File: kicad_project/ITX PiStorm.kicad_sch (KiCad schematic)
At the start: 10 parts, among them J2 USB_67298-4090, J3 DB9_Male_MountingHoles, J4 DB9_Male_MountingHoles, J5 HDMI_A_1.4, J6 DB15_Female_HighDensity

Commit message: playground start
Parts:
- added U101: (no value), symbol Memory_Flash:W25Q128JVS
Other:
- sheet Power Supply ports: added +12V, +5V, GND; removed none

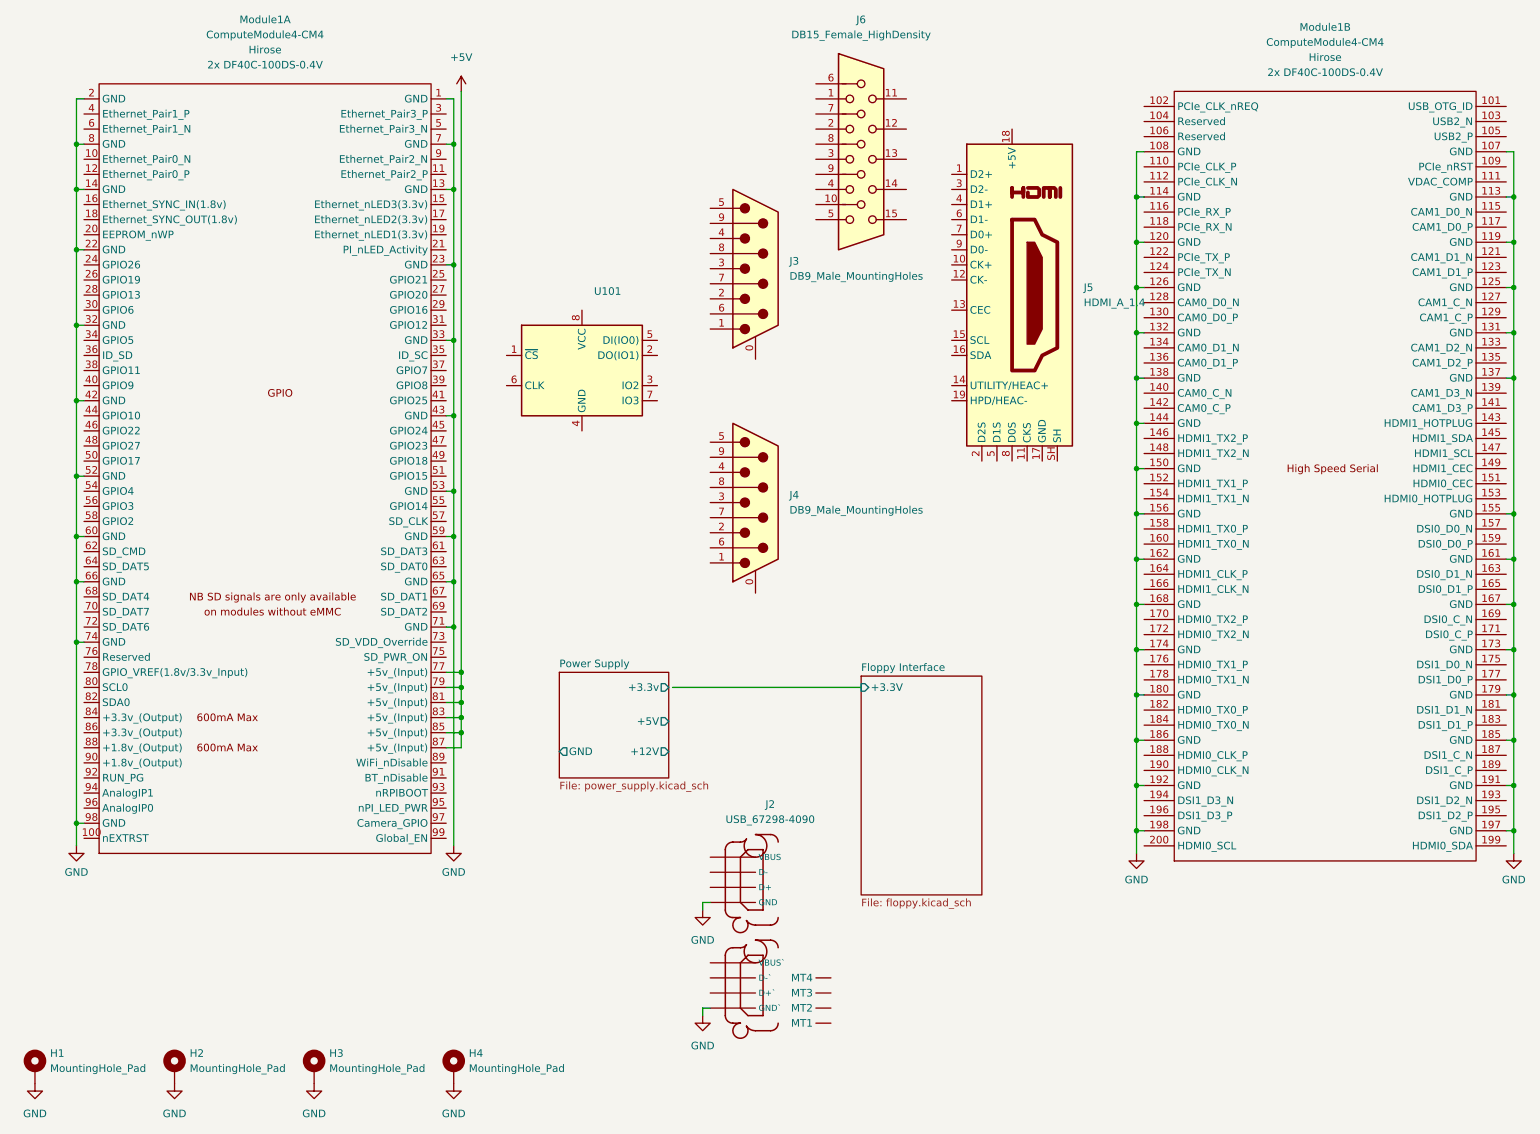
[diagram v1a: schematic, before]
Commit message: added ecp5 fpga without anything connected yet, added power to fpga
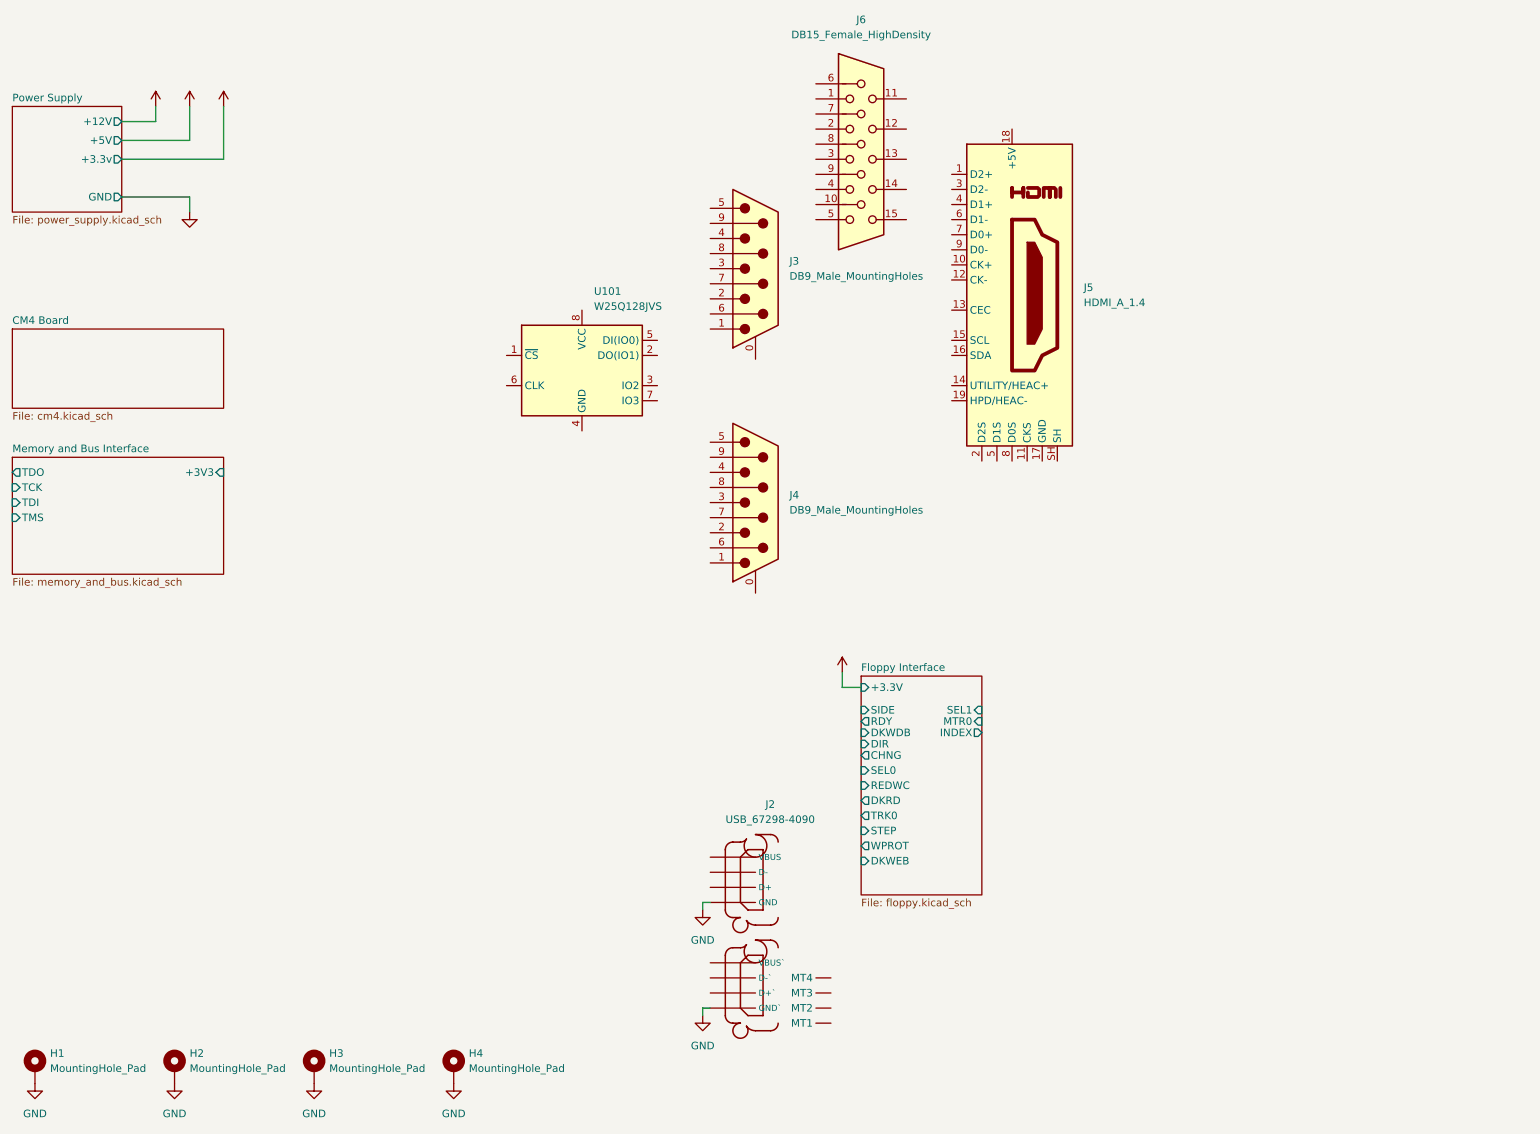
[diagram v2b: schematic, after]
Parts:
- removed Module1: ComputeModule4-CM4, CM4IO:Raspberry-Pi-4-Compute-Module, symbol CM4IO:ComputeModule4-CM4
- U101: value (none) -> W25Q128JVS; footprint (none) -> Package_SO:SOIC-8_5.23x5.23mm_P1.27mm
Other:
- added sheet CM4 Board (cm4.kicad_sch)
- added sheet Memory and Bus Interface (memory_and_bus.kicad_sch)
- sheet Floppy Interface ports: added CHNG, DIR, DKRD, DKWDB, DKWEB, INDEX, MTR0, RDY, REDWC, SEL0, SEL1, SIDE, STEP, TRK0, WPROT; removed none

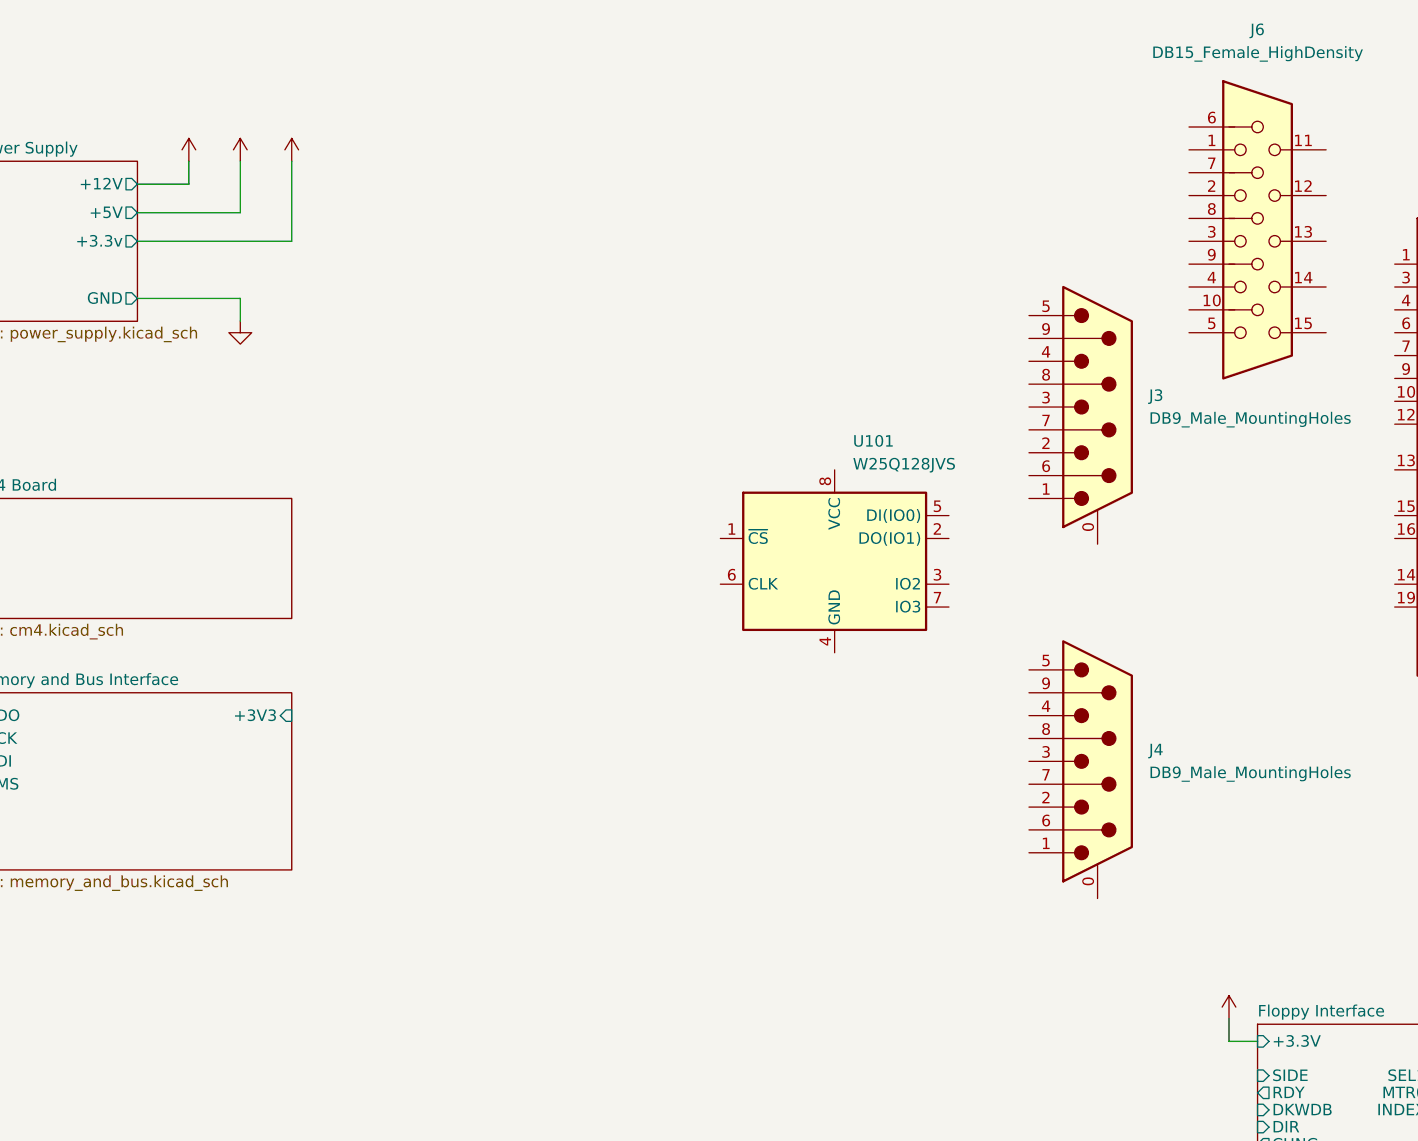
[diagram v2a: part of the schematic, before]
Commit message: added bits and pieces: a bit of memory, a bit of 1.1V power
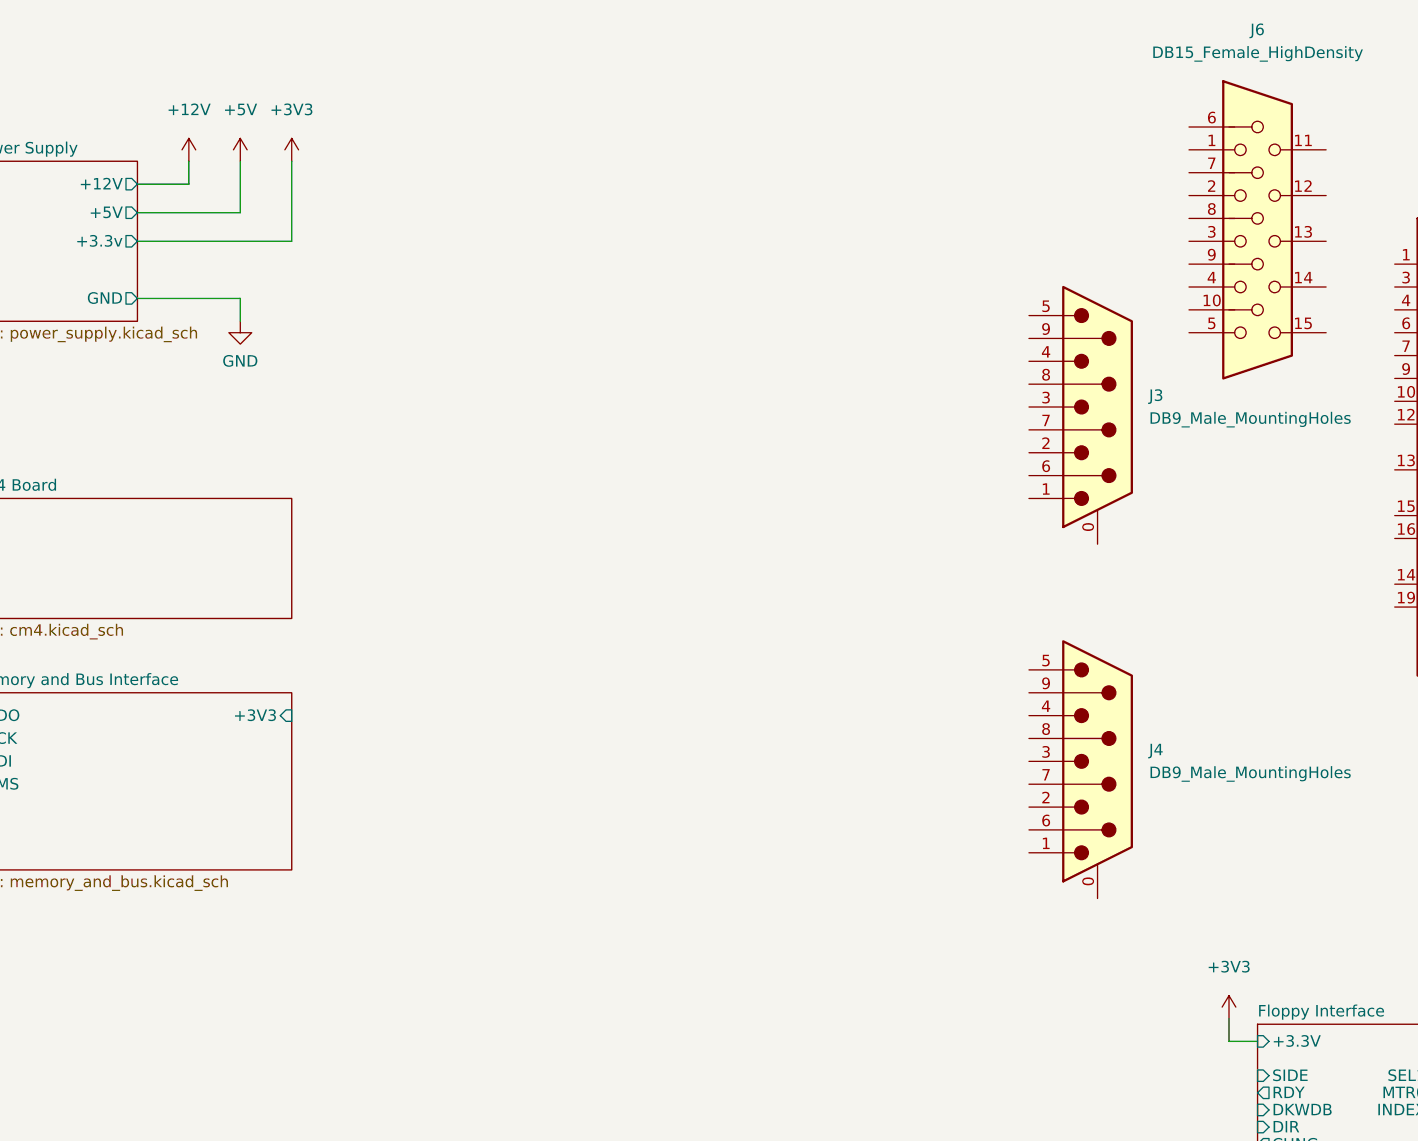
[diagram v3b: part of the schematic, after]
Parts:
- removed U101: W25Q128JVS, Package_SO:SOIC-8_5.23x5.23mm_P1.27mm, symbol Memory_Flash:W25Q128JVS

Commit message: Wip commit
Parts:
- added J1: Micro_SD_Card_Det, Connector_Card:microSD_HC_Hirose_DM3D-SF, symbol Connector:Micro_SD_Card_Det
- added U1: TPS2065CDBVT, TPS2065:Texas_Instruments-DBV0005A-0-0-IPC_B, symbol TPS2065:TPS2065CDBVT
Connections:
- net GND: now also J1.6 (VSS)
- new net CM4 Board/SD_CLK: J1.5 (CLK)
- new net CM4 Board/SD_CMD: J1.3 (CMD)
- new net CM4 Board/SD_DAT0: J1.7 (DAT0)
- new net CM4 Board/SD_DAT1: J1.8 (DAT1)
- new net CM4 Board/SD_DAT2: J1.1 (DAT2)
- new net CM4 Board/SD_DAT3: J1.2 (DAT3/CD)
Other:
- sheet CM4 Board ports: added SD_CLK, SD_CMD, SD_DAT0, SD_DAT1, SD_DAT2, SD_DAT3; removed none
